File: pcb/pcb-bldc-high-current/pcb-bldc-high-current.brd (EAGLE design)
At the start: 50 x 50 mm, 87 parts, among them Q1 MOSFET_NHL60N04D, Q2 MOSFET_NHL60N04D, Q3 MOSFET_NHL60N04D, Q4 MOSFET_NHL60N04D, Q5 MOSFET_NHL60N04D, Q6 MOSFET_NHL60N04D, U1 AS5600, U2 LCT485_BUS_TRANSCEIVER, U3 LCT485_BUS_TRANSCEIVER, U4 HX712_CURR_SENS, U5 STM32G070RBT6, U6 LDO-HT71XX, U7 LDO-HT71XX, X1 PIN_3X2HD, X2 PIN_1X1WELDINGTERMINAL, X3 PIN_1X1WELDINGTERMINAL, X4 PIN_1X1WIRE1, X5 PIN_5X1HD, X6 PIN_1X1WIRE1, X7 PIN_1X1WIRE1, X9 06-JST-B6B-XH-A, Y1 3213-QUARZ3225

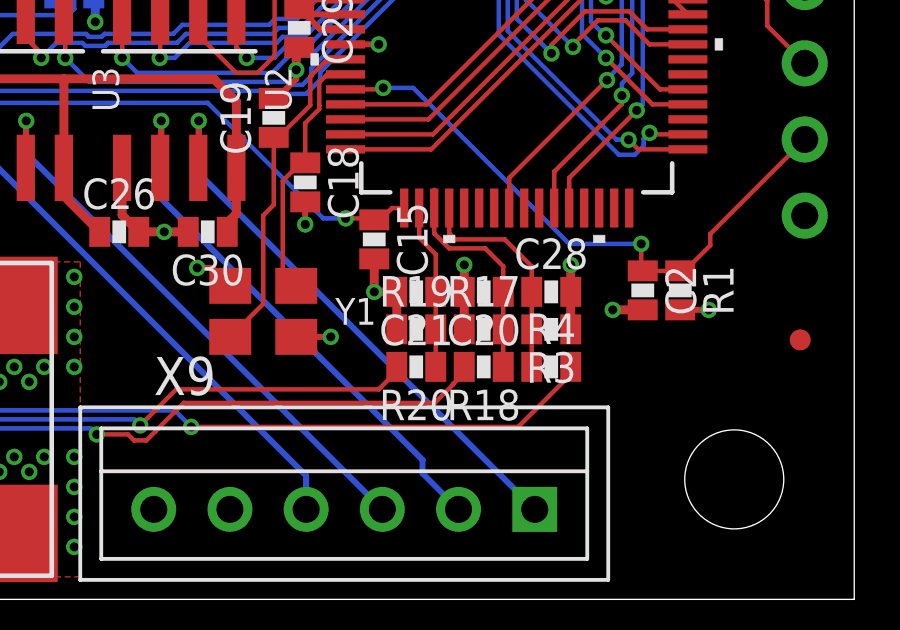
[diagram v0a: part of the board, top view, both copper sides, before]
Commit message: 2 rs485 drivers
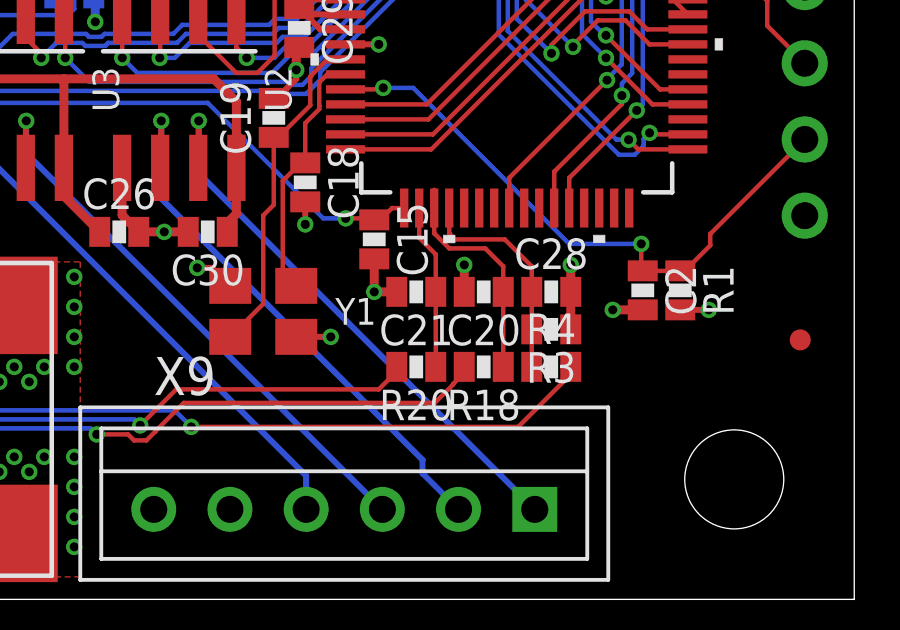
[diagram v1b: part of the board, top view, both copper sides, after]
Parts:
- removed R17, R19: 10k, passives:0603-RES
- Q1, Q2, Q3, Q4, Q5, Q6: value MOSFET_NHL60N04D -> N_MOSFET_PDFN3x3
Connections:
- net +3V3: now also C25.1, U4.8
- net +5V: no longer C25.1, U4.8
- net GND: no longer R17.1, R19.1
- net N$41: no longer R17.2
- net N$42: no longer R19.2
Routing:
- net +3V3: track 30.1 -> 48.1 mm
- net +5V: track 52.1 -> 34.1 mm
- net GND: track 54.0 -> 51.5 mm
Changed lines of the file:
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@@
 <setting verticaltext="up"/>
 </settings>
-<grid distance="0.25" unitdist="mm" unit="mm" style="lines" multiple="1" display="no" altdistance="0.1" altunitdist="mm" altunit="mm"/>
+<grid distance="1" unitdist="mm" unit="mm" style="lines" multiple="1" display="no" altdistance="0.1" altunitdist="mm" altunit="mm"/>
 <layers>
 <layer number="1" name="Top" color="4" fill="1" visible="yes" active="yes"/>
@@
 <attribute name="NAME" x="43.135" y="28.9728" size="1.27" layer="27" ratio="6" rot="SR90"/>
 </element>
-<element name="Q1" library="ftobler" package="DFN3X3-8L" value="MOSFET_NHL60N04D" x="32" y="32" smashed="yes" rot="R270">
+<element name="Q1" library="ftobler" package="DFN3X3-8L" value="N_MOSFET_PDFN3x3" x="32" y="32" smashed="yes" rot="R270">
 <attribute name="NAME" x="32" y="29.46" size="0.889" layer="48" rot="R270"/>
 </element>
@@
 <attribute name="NAME" x="45.038815625" y="36.5388125" size="1.016" layer="25" font="vector" ratio="12" rot="R315" align="bottom-center"/>
 </element>
-<element name="Q2" library="ftobler" package="DFN3X3-8L" value="MOSFET_NHL60N04D" x="25" y="32" smashed="yes" rot="R270">
+<element name="Q2" library="ftobler" package="DFN3X3-8L" value="N_MOSFET_PDFN3x3" x="25" y="32" smashed="yes" rot="R270">
 <attribute name="NAME" x="25" y="29.46" size="0.889" layer="48" rot="R270"/>
 </element>
-<element name="Q3" library="ftobler" package="DFN3X3-8L" value="MOSFET_NHL60N04D" x="18" y="32" smashed="yes" rot="R270">
+<element name="Q3" library="ftobler" package="DFN3X3-8L" value="N_MOSFET_PDFN3x3" x="18" y="32" smashed="yes" rot="R270">
 <attribute name="NAME" x="18" y="29.46" size="0.889" layer="48" rot="R270"/>
 </element>
-<element name="Q4" library="ftobler" package="DFN3X3-8L" value="MOSFET_NHL60N04D" x="32" y="38" smashed="yes" rot="R270">
+<element name="Q4" library="ftobler" package="DFN3X3-8L" value="N_MOSFET_PDFN3x3" x="32" y="38" smashed="yes" rot="R270">
 <attribute name="NAME" x="32" y="35.46" size="0.889" layer="48" rot="R270"/>
 </element>
-<element name="Q5" library="ftobler" package="DFN3X3-8L" value="MOSFET_NHL60N04D" x="25" y="38" smashed="yes" rot="R270">
+<element name="Q5" library="ftobler" package="DFN3X3-8L" value="N_MOSFET_PDFN3x3" x="25" y="38" smashed="yes" rot="R270">
 <attribute name="NAME" x="25" y="35.46" size="0.889" layer="48" rot="R270"/>
 </element>
-<element name="Q6" library="ftobler" package="DFN3X3-8L" value="MOSFET_NHL60N04D" x="18" y="38" smashed="yes" rot="R270">
+<element name="Q6" library="ftobler" package="DFN3X3-8L" value="N_MOSFET_PDFN3x3" x="18" y="38" smashed="yes" rot="R270">
 <attribute name="NAME" x="18" y="35.46" size="0.889" layer="48" rot="R270"/>
 </element>
@@
 <attribute name="NAME" x="26.65" y="6.81" size="1.27" layer="21"/>
 </element>
-<element name="R17" library="passives" package="0603-RES" package3d_urn="urn:adsk.eagle:package:36812383/4" value="10k" x="37.65" y="9" smashed="yes">
-<attribute name="NAME" x="37.65" y="9.762" size="1.016" layer="25" font="vector" ratio="12" align="bottom-center"/>
-</element>
 <element name="R18" library="passives" package="0603-RES" package3d_urn="urn:adsk.eagle:package:36812383/4" value="10k" x="37.65" y="7.75" smashed="yes" rot="R180">
 <attribute name="NAME" x="37.65" y="6.988" size="1.016" layer="25" font="vector" ratio="12" rot="R180" align="bottom-center"/>
@@
 <element name="C20" library="passives" package="0603_CAP" package3d_urn="urn:adsk.eagle:package:36813215/3" value="100n" x="37.65" y="10.25" smashed="yes" rot="R180">
 <attribute name="NAME" x="37.65" y="9.488" size="1.016" layer="25" font="vector" ratio="12" rot="R180" align="bottom-center"/>
-</element>
-<element name="R19" library="passives" package="0603-RES" package3d_urn="urn:adsk.eagle:package:36812383/4" value="10k" x="35.4" y="9" smashed="yes">
-<attribute name="NAME" x="35.4" y="9.762" size="1.016" layer="25" font="vector" ratio="12" align="bottom-center"/>
 </element>
 <element name="R20" library="passives" package="0603-RES" package3d_urn="urn:adsk.eagle:package:36812383/4" value="10k" x="35.4" y="7.75" smashed="yes" rot="R180">
@@
 <contactref element="U2" pad="5"/>
 <contactref element="X9" pad="P$6"/>
-<contactref element="R17" pad="1"/>
 <contactref element="C20" pad="2"/>
-<contactref element="R19" pad="1"/>
 <contactref element="C21" pad="2"/>
 <contactref element="R3" pad="1"/>
@@
 <via x="34" y="10.25" extent="1-16" drill="0.3"/>
 <wire x1="34" y1="11.35" x2="34" y2="10.25" width="0.3" layer="1"/>
-<wire x1="34.75" y1="10.25" x2="34.75" y2="9" width="0.3" layer="1"/>
-<wire x1="37" y1="10.25" x2="37" y2="9" width="0.3" layer="1"/>
 <wire x1="37" y1="10.25" x2="37" y2="11.15" width="0.3" layer="1"/>
 <via x="37" y="11.15" extent="1-16" drill="0.3"/>
@@
 <wire x1="26.35466875" y1="24.265" x2="26.905" y2="23.71466875" width="0.3" layer="16"/>
 <wire x1="26.905" y1="23.71466875" x2="26.905" y2="22.3838" width="0.3" layer="16"/>
+<contactref element="U4" pad="8"/>
+<contactref element="C25" pad="1"/>
+<wire x1="1.25" y1="18.1" x2="2.5788" y2="18.1" width="0.3" layer="1"/>
+<wire x1="2.5788" y1="18.1" x2="2.595" y2="18.1162" width="0.3" layer="1"/>
+<wire x1="2.595" y1="18.1162" x2="2.595" y2="18.995" width="0.3" layer="1"/>
+<wire x1="2.595" y1="18.995" x2="4.15" y2="20.55" width="0.3" layer="1"/>
+<wire x1="4.15" y1="20.55" x2="12.65" y2="20.55" width="0.3" layer="1"/>
+<wire x1="12.65" y1="20.55" x2="13.2" y2="20" width="0.3" layer="1"/>
+<wire x1="13.2" y1="20" x2="13.2" y2="15.72" width="0.3" layer="1"/>
 <wire x1="31.5" y1="19.7" x2="31.65" y2="19.55" width="0" layer="19" extent="1-1"/>
+<wire x1="13.2" y1="15.72" x2="17.2" y2="13.9" width="0" layer="19" extent="1-1"/>
 </signal>
 <signal name="NRST">
@@
 <contactref element="U7" pad="2@1"/>
 <contactref element="C22" pad="1"/>
-<contactref element="U4" pad="8"/>
-<contactref element="C25" pad="1"/>
 <contactref element="C26" pad="1"/>
 <contactref element="C30" pad="1"/>
@@
 <wire x1="29.405" y1="12.855" x2="29.1" y2="12.55" width="0.3" layer="1"/>
 <wire x1="29.405" y1="12.855" x2="29.405" y2="14.3838" width="0.3" layer="1"/>
-<wire x1="1.25" y1="18.1" x2="2.5788" y2="18.1" width="0.3" layer="1"/>
-<wire x1="2.5788" y1="18.1" x2="2.595" y2="18.1162" width="0.3" layer="1"/>
-<wire x1="2.595" y1="18.1162" x2="2.595" y2="18.995" width="0.3" layer="1"/>
-<wire x1="2.595" y1="18.995" x2="4.15" y2="20.55" width="0.3" layer="1"/>
-<wire x1="4.15" y1="20.55" x2="12.65" y2="20.55" width="0.3" layer="1"/>
-<wire x1="12.65" y1="20.55" x2="13.2" y2="20" width="0.3" layer="1"/>
-<wire x1="13.2" y1="20" x2="13.2" y2="15.72" width="0.3" layer="1"/>
 <wire x1="15.7" y1="13.9" x2="16.3" y2="15.1" width="0.5" layer="1"/>
 <wire x1="16.3" y1="15.1" x2="16.45" y2="16.023" width="0.5" layer="1"/>
@@
 <wire x1="12.999" y1="15.519" x2="13.75" y2="13.9" width="0.5" layer="1"/>
 <wire x1="28.65" y1="17.35" x2="23.655" y2="17.35" width="0.3" layer="1"/>
-<wire x1="13.2" y1="15.72" x2="12.999" y2="15.519" width="0" layer="19" extent="1-1"/>
 </signal>
 <signal name="I2C2_SDA">
@@
 </signal>
 <signal name="N$41">
-<contactref element="R17" pad="2"/>
 <contactref element="R18" pad="1"/>
 <contactref element="C20" pad="1"/>
@@
 <wire x1="36" y1="13.04415" x2="36" y2="13.6533" width="0.15" layer="1"/>
 <wire x1="38.3" y1="10.25" x2="38.3" y2="10.2" width="0.15" layer="1"/>
-<wire x1="38.3" y1="10.2" x2="38.3" y2="9" width="0.15" layer="1"/>
-<wire x1="38.3" y1="9" x2="38.3" y2="7.75" width="0.15" layer="1"/>
 <wire x1="36" y1="13.04415" x2="36" y2="12.2" width="0.15" layer="1"/>
 <wire x1="38.3" y1="11.1" x2="38.3" y2="10.25" width="0.15" layer="1"/>
@@
 <wire x1="36.5" y1="11.7" x2="37.7" y2="11.7" width="0.15" layer="1"/>
 <wire x1="37.7" y1="11.7" x2="38.3" y2="11.1" width="0.15" layer="1"/>
+<wire x1="38.3" y1="10.25" x2="38.3" y2="7.75" width="0.15" layer="1"/>
 </signal>
 <signal name="N$42">
-<contactref element="R19" pad="2"/>
 <contactref element="R20" pad="1"/>
 <contactref element="C21" pad="1"/>
 <contactref element="U5" pad="18"/>
-<wire x1="36.05" y1="10.25" x2="36.05" y2="9" width="0.15" layer="1"/>
-<wire x1="36.05" y1="9" x2="36.05" y2="7.75" width="0.15" layer="1"/>
 <wire x1="35.5" y1="13.04415" x2="35.5" y2="12.05" width="0.15" layer="1"/>
 <wire x1="36.05" y1="11.5" x2="36.05" y2="10.25" width="0.15" layer="1"/>
 <wire x1="35.5" y1="12.05" x2="36.05" y2="11.5" width="0.15" layer="1"/>
+<wire x1="36.05" y1="10.25" x2="36.05" y2="7.75" width="0.15" layer="1"/>
 </signal>
 <signal name="N$43">

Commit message: pcb release high current
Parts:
- removed C30: 100n, passives:0603_CAP
- removed X9: 06-JST-B6B-XH-A, bt_con-jst-xh:B6B-XH
- added C31, C32: 100n, passives:0603_CAP
- added J2: GT-USB-7010, ftobler:GT-USB-7010
- added R17, R19: 5k1, passives:0603-RES
- added R21, R22: 4k7, passives:0603-RES
- added R23, R24: 100, passives:0603-RES
- added U$4: 03-JST-B3B-XH-A, bt_con-jst-xh:B3B-XH
- U$2: value LOGO-TOBENG-4MM-MASK -> LOGO-0.25MM; device ftobler:TOBENG-4MM-MASK -> ftobler:LOGO-0.25MM
- U3: value LCT485_BUS_TRANSCEIVER -> CH340X; device ftobler:SOIC-8 -> ftobler:MSOP-10
- moved U$2 49.2 mm to (44.2, 8.50)
- moved U$1 36.0 mm to (7.55, 38.9)
- moved R20 35.3 mm to (1.05, 15.9), turned to 90 degrees
- moved R18 31.5 mm to (8.05, 18.6), turned to 90 degrees
- moved R4 20.8 mm to (48.1, 26.9)
- moved R3 18.5 mm to (48.1, 25.6)
- moved U3 9.80 mm to (28.9, 10.3)
- moved Y1 8.16 mm to (27.9, 17.4), turned to 270 degrees
- moved U2 5.75 mm to (21.8, 17.0)
- moved V1 2.93 mm to (12.4, 48.5)
- moved C18 2.15 mm to (30.9, 15.9), turned to 0 degrees
- moved C26 1.98 mm to (25.1, 14.2), turned to 90 degrees
- moved C19 1.87 mm to (30.1, 17.9)
- moved C15 1.39 mm to (32.8, 12.7), turned to 180 degrees
- moved C2 1.24 mm to (43.9, 11.1)
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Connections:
- removed net N$38: U3.7, X9.P$3
- removed net N$39: U3.6, X9.P$4
- new net 485A: U$4.P$2, U2.6
- new net 485B: U$4.P$1, U2.7
- new net DTR: R22.1, U3.6, U5.3
- new net N$51: J2.B5, R17.2
- new net N$52: J2.A5, R19.2
- new net N$53: C31.1, U3.10
- new net USB_N: J2.A7, J2.B7, U3.2
- new net USB_P: J2.A6, J2.B6, U3.1
- net +3V3: no longer X9.P$5
- net +5V: no longer C30.1, U3.8
- net GND: now also C31.2, C32.2, J2.13, J2.14, J2.15, J2.16, J2.A1B12, J2.B1A12, J2.PAD1, J2.PAD2, J2.PAD3, J2.PAD4, J2.PAD5, J2.PAD6, R17.1, R19.1, R22.2, U$4.P$3, U3.3; no longer C30.2, U3.5, X9.P$6
- net N$1: now also R23.2, U3.8; no longer U2.2, U5.3
- net N$36: now also C32.1, J2.A4B9, J2.B4A9, U3.7; no longer U2.7, X9.P$1
- net N$37: now also R21.2, U3.4; no longer U2.6, X9.P$2
- net N$45: now also U2.1; no longer U3.1
- net N$46: now also U2.2; no longer U3.2
- net N$47: now also U2.3; no longer U3.3
- net N$48: now also U2.4; no longer U3.4
- net N$5: now also R24.2, U3.9; no longer U2.3, U5.2
- net NRST: now also R21.1
- net USART1_RX: now also R23.1; no longer U2.1
- net USART1_TX: now also R24.1; no longer U2.4
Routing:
- net N$41: track 7.61 -> 53.2 mm, vias 0 -> 2
- net N$42: track 5.52 -> 50.3 mm, vias 0 -> 2
- net N$43: track 43.7 -> 5.21 mm, vias 2 -> 0
- net N$44: track 42.0 -> 4.58 mm, vias 2 -> 1
- net VCC: track 46.7 -> 15.6 mm, vias 61 -> 60
- net GND: track 51.5 -> 79.4 mm, vias 144 -> 148
- net 485A: track 0.00 -> 24.5 mm, vias 0 -> 1
- net 485B: track 0.00 -> 24.1 mm, vias 0 -> 1
- net N$38: track 19.4 -> 0.00 mm, vias 1 -> 0
- net N$39: track 18.9 -> 0.00 mm, vias 1 -> 0
- net VCCMEAS: track 7.40 -> 26.1 mm, vias 0 -> 2
- net DTR: track 0.00 -> 18.5 mm
- net N$37: track 18.6 -> 1.33 mm, vias 1 -> 0
- net +5V: track 34.1 -> 22.5 mm
- net N$52: track 0.00 -> 11.3 mm, vias 0 -> 2
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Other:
- board text added: "+"
- board text added: "12V"
- board text added: "25V 680uF d=10mm"
- board text added: "A"
- board text added: "B"
- board text added: "DRV8300"
- board text added: "FD6187T"
- board text added: "GND"
- board text added: "LTC485"
- board text added: "STM32 G070RBT"
- board text added: "U"
- board text added: "V"
- board text added: "W"
- board text added: "pcb-bldc- high-current v1 2024 by ftobler"
